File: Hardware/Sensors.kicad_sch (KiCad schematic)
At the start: 60 parts, among them J10 VL53L0X, J11 VL53L0X, J12 VL53L0X, J13 VL53L0X, J8 VL53L0X, J9 VL53L0X, Q10 Q_NMOS_GSD, Q11 Q_NMOS_GSD, Q12 Q_NMOS_GSD, Q13 TEFT4300, Q2 Q_NMOS_GSD, Q3 TEFT4300, Q4 TEFT4300, Q5 TEFT4300, Q6 TEFT4300, Q7 TEFT4300, Q8 Q_NMOS_GSD, Q9 Q_NMOS_GSD

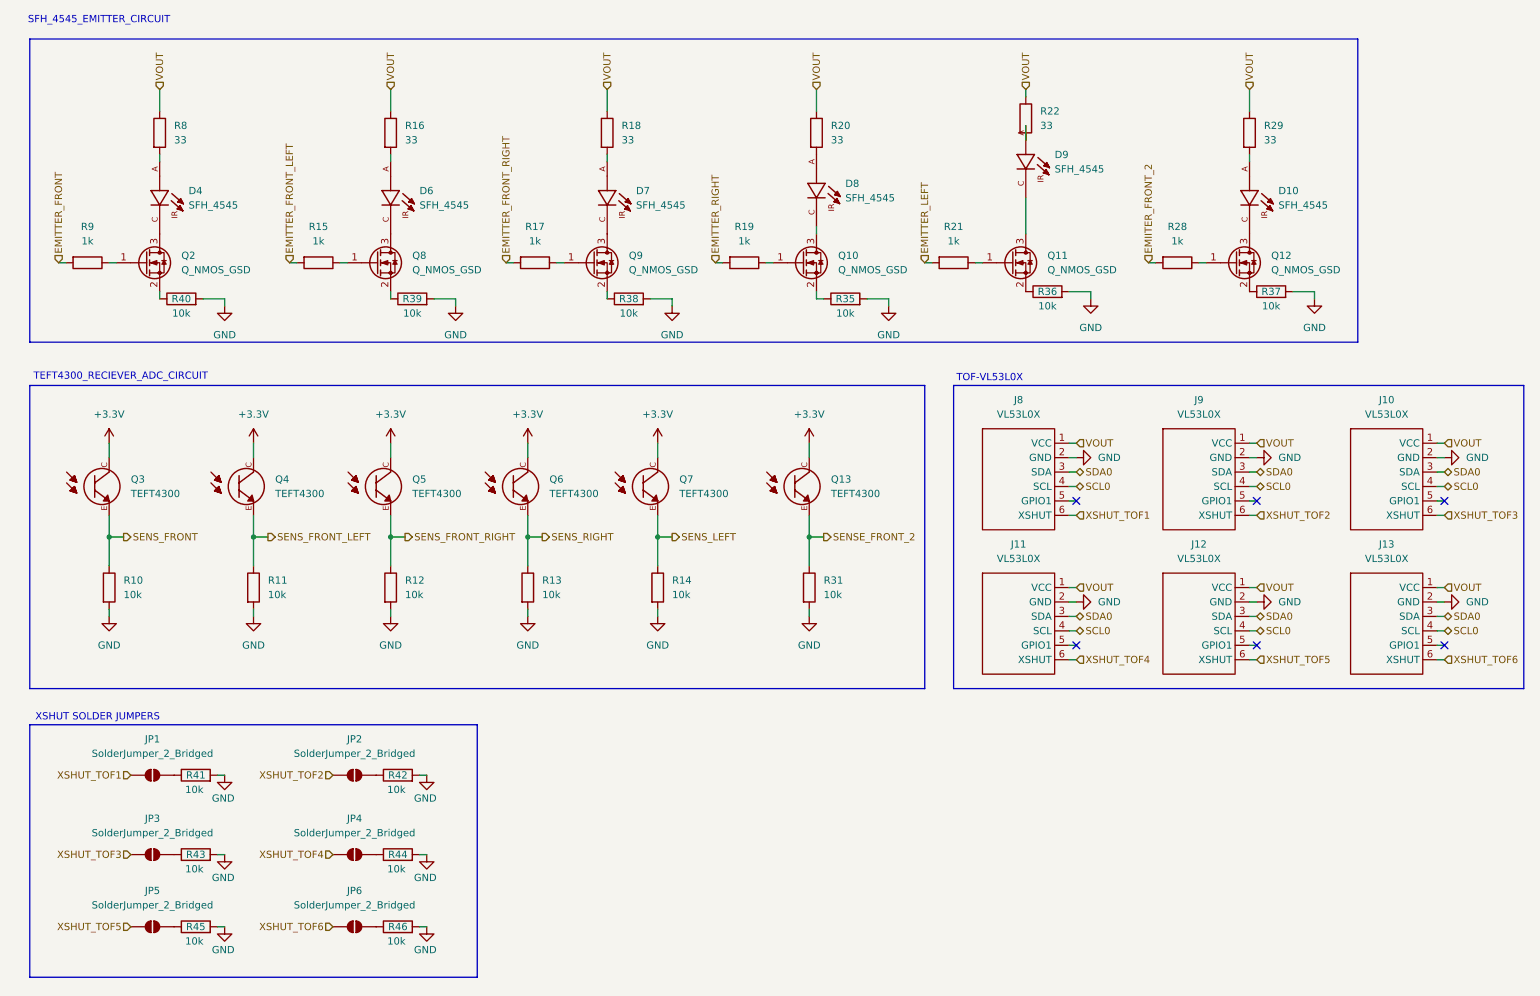
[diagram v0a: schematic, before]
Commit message: Schematic updated with buck and motor driver breakout boards
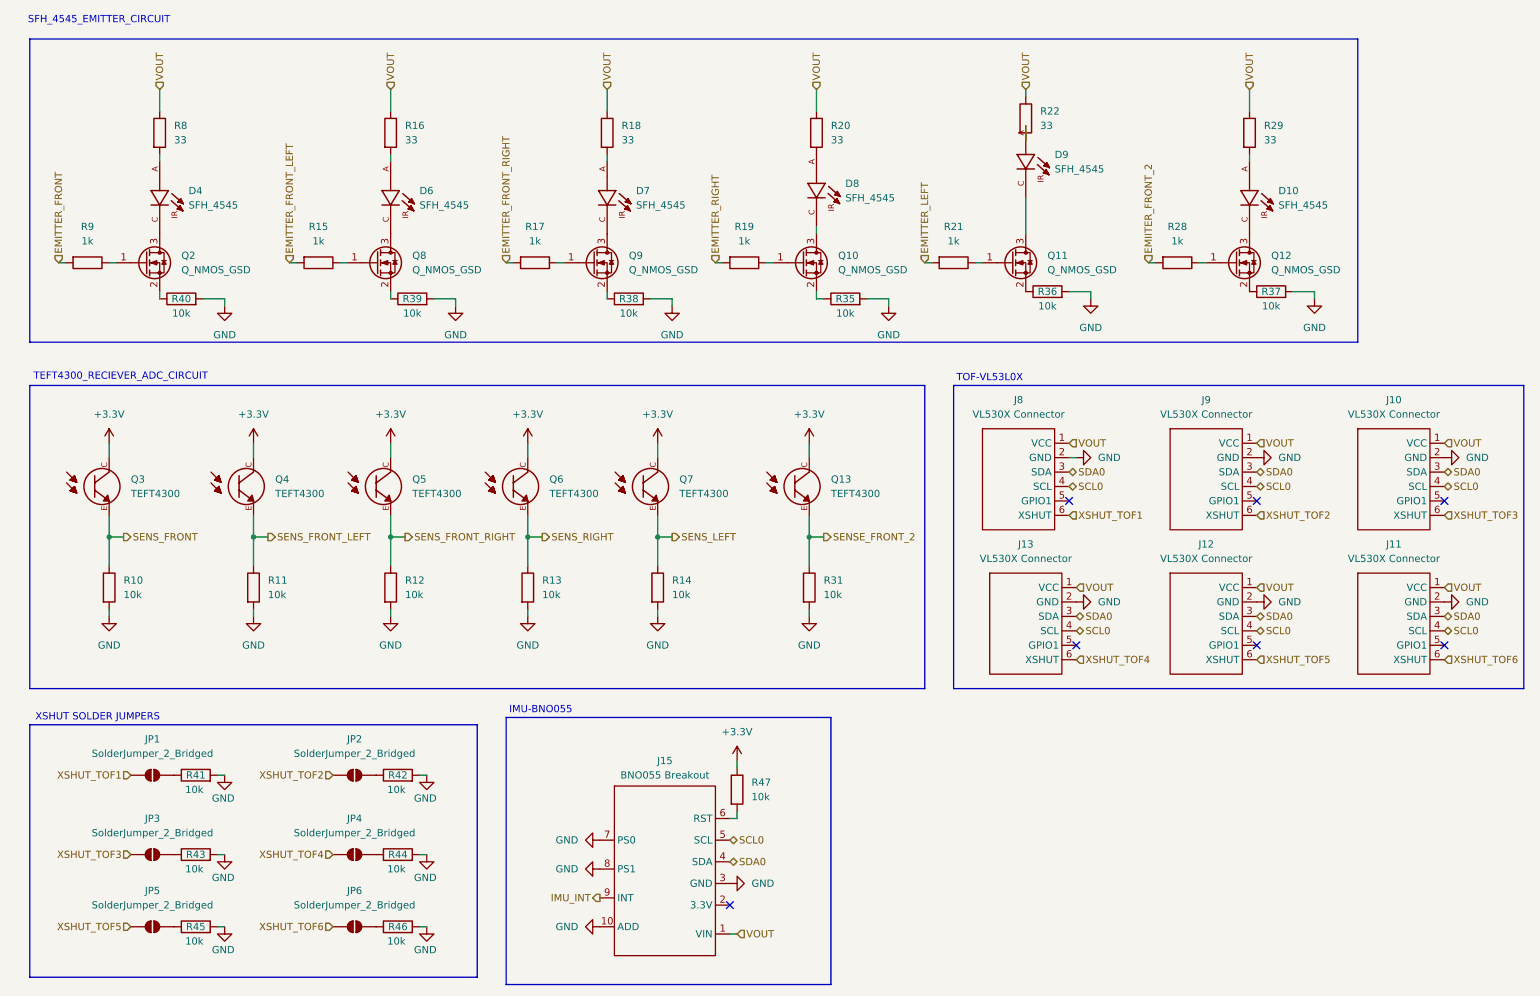
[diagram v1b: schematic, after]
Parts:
- removed J10, J11, J12, J13, J8, J9: VL53L0X, symbol micromouse_custom:VL53L0X
- added J10, J11, J12, J13, J8, J9: VL530X Connector, symbol HSM_Symbols:VL530X
- added J15: BNO055 Breakout, symbol HSM_Symbols:BNO055_Breakout_Board
- added R47: 10k, symbol Device:R
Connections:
- net +3.3V: now also R47.1
- net GND: now also J10.2 (GND), J11.2 (GND), J12.2 (GND), J13.2 (GND), J15.10 (ADD), J15.3 (GND), J15.7 (PS0), J15.8 (PS1), J8.2 (GND), J9.2 (GND)
- net SCL0: now also J10.4 (SCL), J11.4 (SCL), J12.4 (SCL), J13.4 (SCL), J15.5 (SCL), J8.4 (SCL), J9.4 (SCL)
- net SDA0: now also J10.3 (SDA), J11.3 (SDA), J12.3 (SDA), J13.3 (SDA), J15.4 (SDA), J8.3 (SDA), J9.3 (SDA)
- net VOUT: now also J10.1 (VCC), J11.1 (VCC), J12.1 (VCC), J13.1 (VCC), J15.1 (VIN), J8.1 (VCC), J9.1 (VCC)
- net XSHUT_TOF1: now also J8.6 (XSHUT)
- net XSHUT_TOF2: now also J9.6 (XSHUT)
- net XSHUT_TOF3: now also J10.6 (XSHUT)
- net XSHUT_TOF4: now also J13.6 (XSHUT)
- net XSHUT_TOF5: now also J12.6 (XSHUT)
- net XSHUT_TOF6: now also J11.6 (XSHUT)
- new net: J15.6 (RST), R47.2
- new net IMU_INT: J15.9 (INT)
- no-connect marks 6 -> 7
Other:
- note added: "IMU-BNO055"

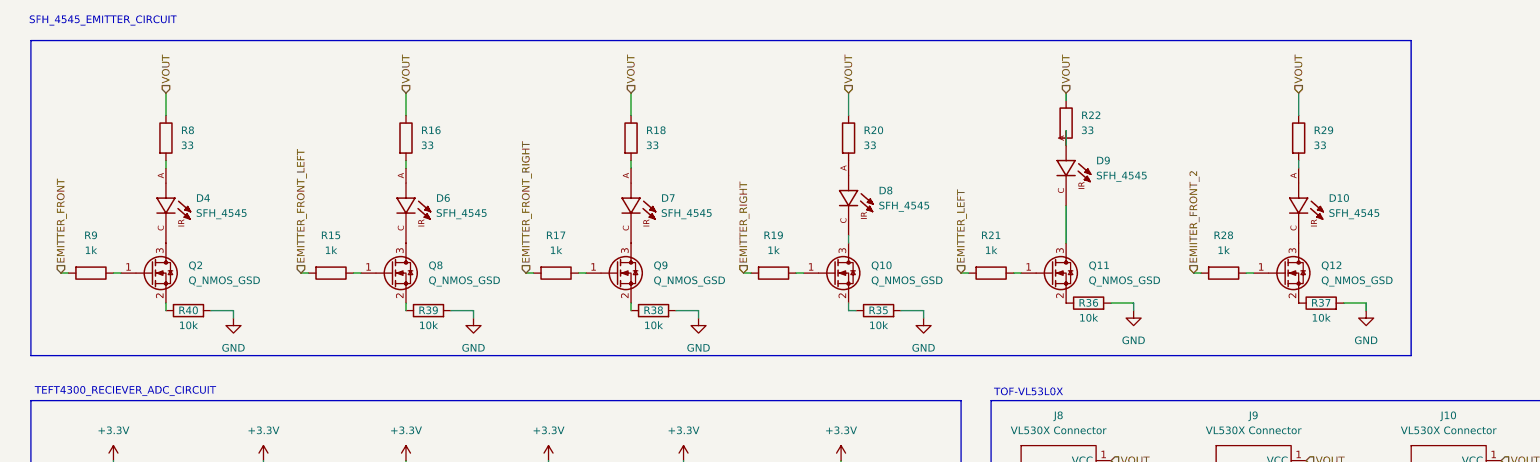
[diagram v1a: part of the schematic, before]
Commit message: Switches changed,added low pass filters, emitter caps
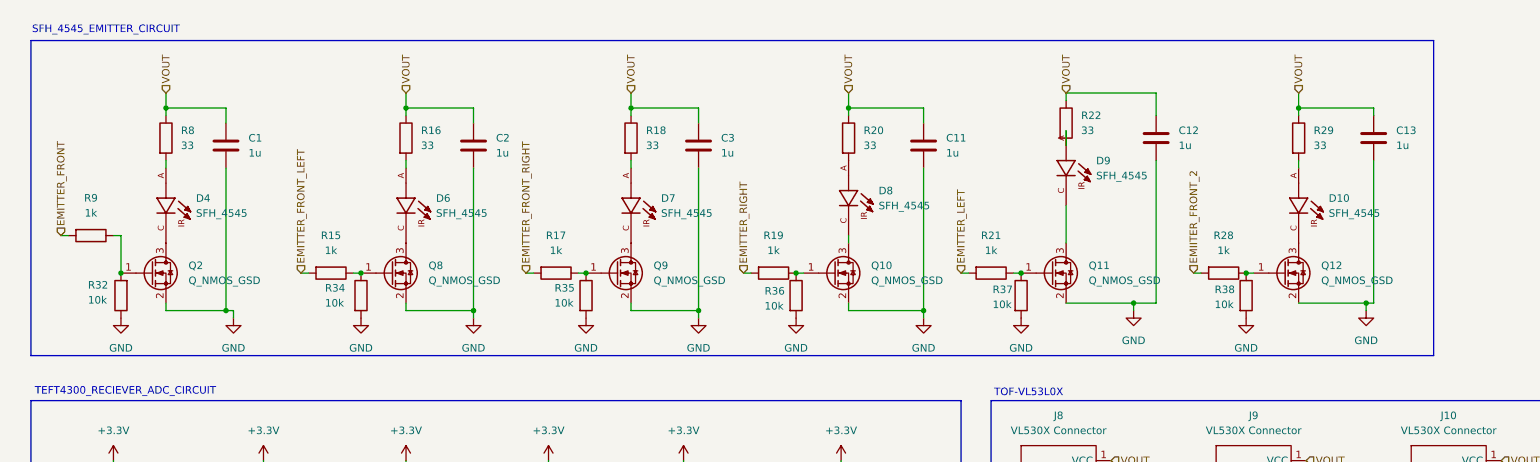
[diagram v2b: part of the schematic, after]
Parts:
- removed R39, R40: 10k, symbol Device:R
- added C1, C11, C12, C13, C2, C3: 1u, Capacitor_SMD:C_0603_1608Metric, symbol Device:C
- added R32, R34: 10k, Resistor_SMD:R_0603_1608Metric, symbol Device:R
- D10, D4, D6, D7, D8, D9: footprint SFH_4545:DIO_SFH_4545 -> LED_THT:LED_D5.0mm
- J10, J11, J12, J13, J8, J9: footprint (none) -> Connector_PinSocket_2.54mm:PinSocket_1x06_P2.54mm_Vertical
- J15: footprint (none) -> Micromouse_Footprints:BNO055
- JP1, JP2, JP3, JP4, JP5, JP6: footprint (none) -> Jumper:SolderJumper-2_P1.3mm_Open_RoundedPad1.0x1.5mm
- Q10, Q11, Q12, Q2, Q8, Q9: footprint (none) -> Package_TO_SOT_SMD:SOT-23
- Q13, Q3, Q4, Q5, Q6, Q7: footprint TEFT4300:XDCR_TEFT4300 -> LED_THT:LED_D3.0mm
- R10, R11, R12, R13, R14, R15, R16, R17, R18, R19, R20, R21, R22, R28, R29, R31, R35, R36, R37, R38, R41, R42, R43, R44, R45, R46, R47, R8, R9: footprint (none) -> Resistor_SMD:R_0603_1608Metric
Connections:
- net GND: now also Q10.2 (S), Q11.2 (S), Q12.2 (S), Q2.2 (S), Q8.2 (S), Q9.2 (S), C1.2, C11.2, C12.2, C13.2, C2.2, C3.2, R32.1, R34.2
- net VOUT: now also C1.1, C11.1, C12.1, C13.1, C2.1, C3.1
- net at Q9.1 (G), R17.1: now also R35.1
- net at R38.1: now also Q12.1 (G), R28.1; no longer Q9.2 (S)
- net at R36.1: now also Q10.1 (G), R19.1; no longer Q11.2 (S)
- net at Q2.1 (G), R9.1: now also R32.2
- net at R37.1: now also Q11.1 (G), R21.1; no longer Q12.2 (S)
- net at Q8.1 (G), R15.1: now also R34.1
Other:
- moved on the sheet: R9

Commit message: Added KiCad PCB files
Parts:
- removed D10: SFH_4545, LED_THT:LED_D5.0mm, symbol SFH_4545:SFH_4545
- added D1: SFH_4545, LED_THT:LED_D5.0mm, symbol SFH_4545:SFH_4545
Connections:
- net +3.3V: now also Q13.2, Q3.2, Q4.2, Q5.2, Q6.2, Q7.2; no longer Q13.C, Q3.C, Q4.C, Q5.C, Q6.C, Q7.C
- net SENSE_FRONT_2: now also Q13.1; no longer Q13.E
- net SENS_FRONT: now also Q3.1; no longer Q3.E
- net SENS_FRONT_LEFT: now also Q4.1; no longer Q4.E
- net SENS_FRONT_RIGHT: now also Q5.1; no longer Q5.E
- net SENS_LEFT: now also Q7.1; no longer Q7.E
- net SENS_RIGHT: now also Q6.1; no longer Q6.E
- net at R8.2: now also D4.2; no longer D4.A
- net at Q9.3 (D): now also D6.1; no longer D7.C
- net at Q10.3 (D): now also D7.1; no longer D8.C
- net at Q2.3 (D): now also D4.1; no longer D4.C
- net at R29.2: now also D9.2
- net at R22.2: now also D8.2; no longer D9.A
- net at Q11.3 (D): now also D8.1; no longer D9.C
- net at Q12.3 (D): now also D9.1
- net at R20.2: now also D7.2; no longer D8.A
- net at R18.2: now also D6.2; no longer D7.A
- net at R16.2: now also D1.2; no longer D6.A
- net at Q8.3 (D): now also D1.1; no longer D6.C

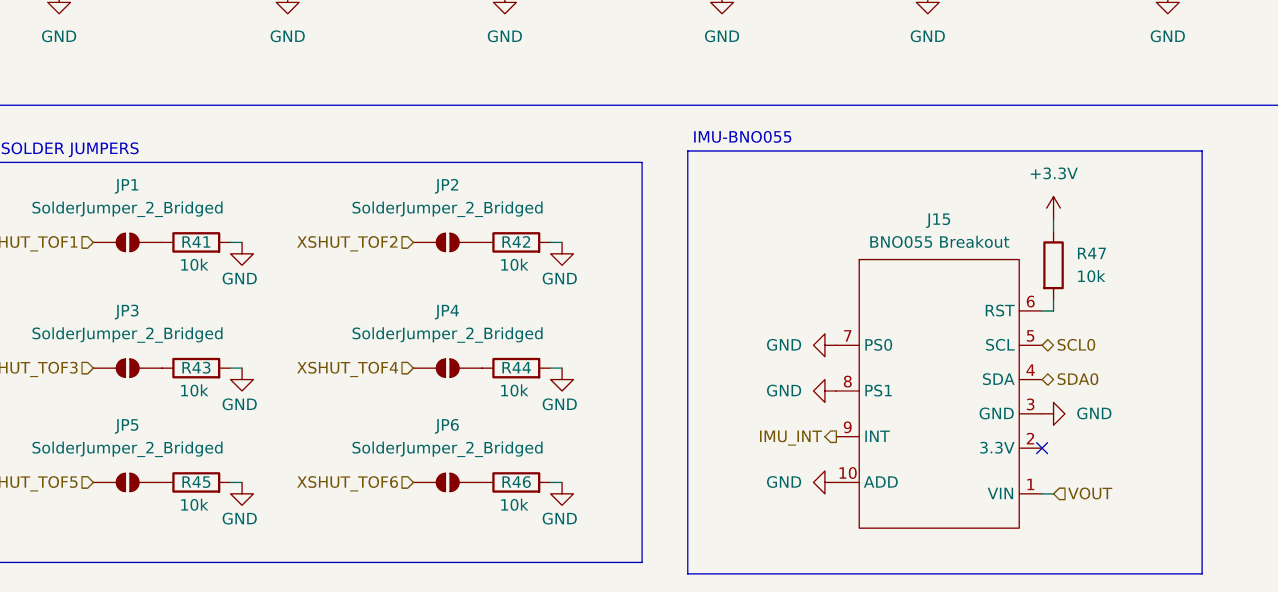
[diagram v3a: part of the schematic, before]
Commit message: Added the mounting holes, kill iwtch for the moto,removed resistors from xshut, and some others
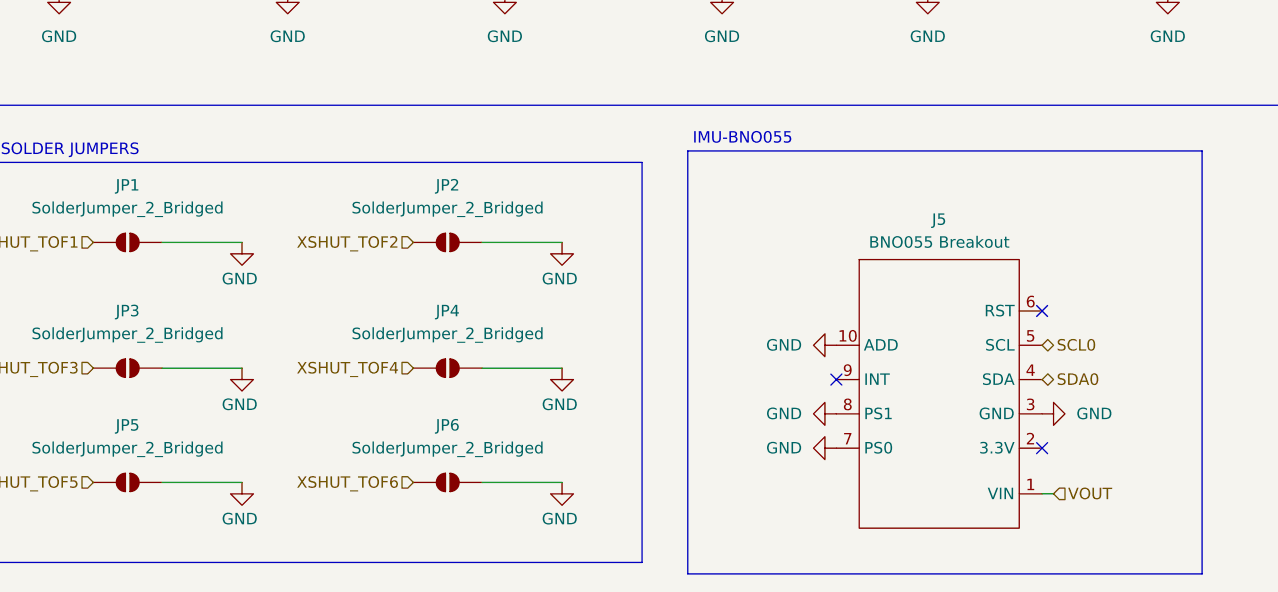
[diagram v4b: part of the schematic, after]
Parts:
- removed J15: BNO055 Breakout, Micromouse_Footprints:BNO055, symbol HSM_Symbols:BNO055_Breakout_Board
- removed R41, R42, R43, R44, R45, R46, R47: 10k, Resistor_SMD:R_0603_1608Metric, symbol Device:R
- added J5: BNO055 Breakout, Micromouse_Footprints:BNO055, symbol HSM_Symbols:BNO055_Breakout_Board
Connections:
- net GND: now also JP1.2 (B), JP2.2 (B), JP3.2 (B), JP4.2 (B), JP5.2 (B), JP6.2 (B), J5.10 (ADD), J5.3 (GND), J5.7 (PS0), J5.8 (PS1)
- net SCL0: now also J5.5 (SCL)
- net SDA0: now also J5.4 (SDA)
- net VOUT: now also J5.1 (VIN)
- no-connect marks 7 -> 9
